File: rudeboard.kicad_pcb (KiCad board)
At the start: 2 copper layers, 295.8 x 124.2 mm, 132 parts, among them U1 Elite-C

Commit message: update to v1.1
changes to schematic:
- potentially better
- more pins used so more dependant on elite-c but more legible

routing:
- looks better than before
- is more dependant on elite-c (or much less on pro micro)

update revision/dates
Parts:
- moved U1 22.1 mm to (254.1, 140.5), turned to 270 degrees
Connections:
- D15 pad 1: row2 -> row0
- D16 pad 1: row3 -> row2
- D17 pad 1: row2 -> row3
- D18 pad 1: row3 -> row2
- D19 pad 1: row2 -> row3
- D20 pad 1: row3 -> row2
- D21 pad 1: row2 -> row3
- D22 pad 1: row3 -> row2
- D23 pad 1: row2 -> row3
- D24 pad 1: row3 -> row2
- D25 pad 1: row2 -> row3
- D26 pad 1: row3 -> row2
- D27 pad 1: row2 -> row3
- D28 pad 1: row3 -> row2
- D42 pad 1: row5 -> row7
- D54 pad 1: row7 -> row8
- D55 pad 1: row6 -> row9
- D56 pad 1: row7 -> row8
- D57 pad 1: row8 -> row9
- D58 pad 1: row9 -> row8
- D59 pad 1: row8 -> row9
- D60 pad 1: row9 -> row8
- D61 pad 1: row8 -> row9
- D62 pad 1: row9 -> row8
- D63 pad 1: row8 -> row10
- D64 pad 1: row9 -> row11
- D65 pad 1: row8 -> row10
- MX10 pad 1: col4 -> col5
- MX12 pad 1: col5 -> col6
- MX14 pad 1: col6 -> col7
- MX15 pad 1: col0 -> col7
- MX2 pad 1: col0 -> col1
- MX22 pad 1: col3 -> col4
- MX24 pad 1: col4 -> col5
- MX25 pad 1: col5 -> col6
- MX26 pad 1: col5 -> col6
- MX27 pad 1: col6 -> col7
- MX28 pad 1: col6 -> col7
- MX30 pad 1: col0 -> col1
- MX32 pad 1: col1 -> col2
- MX34 pad 1: col2 -> col3
- MX35 pad 1: col3 -> col4
- MX36 pad 1: col3 -> col4
- MX37 pad 1: col4 -> col5
- MX38 pad 1: col4 -> col6
- MX39 pad 1: col5 -> col6
- MX4 pad 1: col1 -> col2
- MX40 pad 1: col5 -> col7
- MX41 pad 1: col6 -> col7
- MX42 pad 1: col6 -> col0
- MX43 pad 1: col0 -> col1
- MX44 pad 1: col0 -> col1
- MX45 pad 1: col1 -> col2
- MX46 pad 1: col1 -> col2
- MX47 pad 1: col2 -> col3
- MX48 pad 1: col2 -> col4
- MX49 pad 1: col3 -> col5
- MX50 pad 1: col3 -> col6
- MX51 pad 1: col4 -> col6
- MX52 pad 1: col4 -> col7
- MX53 pad 1: col5 -> col7
- MX54 pad 1: col5 -> col1
- MX55 pad 1: col6 -> col1
- MX56 pad 1: col6 -> col2
- MX57 pad 1: col0 -> col2
- MX58 pad 1: col0 -> col3
- MX59 pad 1: col1 -> col5
- MX6 pad 1: col2 -> col3
- MX60 pad 1: col1 -> col6
- MX61 pad 1: col2 -> col6
- MX62 pad 1: col2 -> col7
- MX63 pad 1: col3 -> col2
- MX65 pad 1: col4 -> col6
- MX8 pad 1: col3 -> col4
- U1 pad 1: Net-(U1-Pad1) -> row0
- U1 pad 10: row3 -> col6
- U1 pad 11: row2 -> row8
- U1 pad 12: row0 -> row9
- U1 pad 13: col2 -> Net-(U1-Pad13)
- U1 pad 14: col6 -> Net-(U1-Pad14)
- U1 pad 15: Net-(U1-Pad15) -> row2
- U1 pad 16: col4 -> row3
- U1 pad 17: col3 -> col4
- U1 pad 18: row7 -> col3
- U1 pad 19: col1 -> col2
- U1 pad 2: Net-(U1-Pad2) -> row1
- U1 pad 20: col0 -> col1
- U1 pad 24: Net-(U1-Pad24) -> col0
- U1 pad 25: row1 -> row10
- U1 pad 26: Net-(U1-Pad26) -> row11
- U1 pad 27: Net-(U1-Pad27) -> col7
- U1 pad 29: col5 -> Net-(U1-Pad29)
- U1 pad 5: row8 -> row7
- U1 pad 6: row9 -> row6
- U1 pad 7: row6 -> row5
- U1 pad 8: row5 -> row4
- U1 pad 9: row4 -> col5
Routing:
- net col7: track 0.00 -> 281.2 mm, vias 0 -> 1
- net col5: track 397.1 -> 126.6 mm, vias 1 -> 0
- net col0: track 504.2 -> 279.5 mm, vias 0 -> 1
- net row10: track 0.00 -> 223.2 mm, vias 0 -> 1
- net col3: track 349.9 -> 189.8 mm, vias 2 -> 1
- net col6: track 396.0 -> 263.3 mm, vias 6 -> 1
- net row5: track 350.7 -> 264.3 mm, vias 8 -> 13
- net col4: track 246.6 -> 167.2 mm, vias 1 -> 0
- net row9: track 167.8 -> 238.7 mm, vias 5 -> 3
- net row7: track 340.0 -> 272.4 mm, vias 3 -> 0
- net col1: track 314.6 -> 375.0 mm, vias 0 -> 1
- net row11: track 0.00 -> 60.3 mm, vias 0 -> 1
- net row6: track 314.5 -> 263.3 mm, vias 4 -> 7
- net row3: track 339.7 -> 295.2 mm, vias 2 -> 13
- net row1: track 332.2 -> 292.9 mm, vias 3 -> 13
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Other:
- net class Default: clearance 0.2 -> 0.25
- rule trace_clearance: 0.2 -> 0.25
- rule trace_min: 0.2 -> 0.0889
- rule via_min_size: 0.4 -> 0.2

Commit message: prep for reroute
- delete all existing routes
- move all diodes to a side of the switch
- clean elite-c footprint
  - remove front silkscreen
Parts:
- moved U1 46.8 mm to (254.1, 93.7)
- moved D59 13.1 mm to (286.4, 150.6), turned to 90 degrees
- moved D47 13.1 mm to (210.2, 131.6), turned to 90 degrees
- moved D64 13.1 mm to (224.5, 169.8), turned to 90 degrees
- moved D63 13.0 mm to (129.2, 169.7), turned to 90 degrees
- moved D39 13.0 mm to (319.7, 112.5), turned to 90 degrees
- moved D51 13.0 mm to (319.7, 131.6), turned to 90 degrees
- moved D65 13.0 mm to (319.7, 169.7), turned to 90 degrees
- moved D44 13.0 mm to (129.2, 131.6), turned to 90 degrees
- moved D57 13.0 mm to (162.4, 150.6), turned to 90 degrees
- moved D61 12.9 mm to (329.1, 150.6), turned to 90 degrees
- moved D55 12.9 mm to (114.8, 150.6), turned to 90 degrees
- moved D16 12.9 mm to (90.9, 93.3), turned to 90 degrees
- moved D49 12.9 mm to (281.4, 131.4), turned to 90 degrees
- moved D12 12.9 mm to (300.5, 74.4), turned to 90 degrees
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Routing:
- net col1: track 375.0 -> 0.00 mm, vias 1 -> 0
- net row2: track 346.0 -> 0.00 mm, vias 1 -> 0
- net row0: track 341.5 -> 0.00 mm, vias 1 -> 0
- net col2: track 333.8 -> 0.00 mm
- net row4: track 314.2 -> 0.00 mm, vias 1 -> 0
- net row8: track 297.2 -> 0.00 mm, vias 2 -> 0
- net row3: track 295.2 -> 0.00 mm, vias 13 -> 0
- net row1: track 292.9 -> 0.00 mm, vias 13 -> 0
- net col7: track 281.2 -> 0.00 mm, vias 1 -> 0
- net col0: track 279.5 -> 0.00 mm, vias 1 -> 0
- net row7: track 272.4 -> 0.00 mm
- net row5: track 264.3 -> 0.00 mm, vias 13 -> 0
- net col6: track 263.3 -> 0.00 mm, vias 1 -> 0
- net row6: track 263.3 -> 0.00 mm, vias 7 -> 0
- net row9: track 238.7 -> 0.00 mm, vias 3 -> 0
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
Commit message: rerouted pcb
- better placement of elite-c
- looks better
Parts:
- moved D64 0.25 mm to (224.5, 169.5)
- moved D22 0.13 mm to (224.3, 93.5)
- moved D23 0.13 mm to (243.3, 93.5)
- moved D24 0.13 mm to (281.4, 93.5)
- moved D25 0.13 mm to (300.5, 93.5)
- moved D26 0.13 mm to (319.5, 93.5)
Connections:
- U1 pad 10: col6 -> row11
- U1 pad 11: row8 -> row10
- U1 pad 15: row2 -> col4
- U1 pad 16: row3 -> col3
- U1 pad 17: col4 -> col2
- U1 pad 18: col3 -> col1
- U1 pad 19: col2 -> row2
- U1 pad 20: col1 -> row3
- U1 pad 25: row10 -> row8
- U1 pad 26: row11 -> row6
- U1 pad 27: col7 -> row7
- U1 pad 28: Net-(U1-Pad28) -> row4
- U1 pad 29: Net-(U1-Pad29) -> row5
- U1 pad 5: row7 -> Net-(U1-Pad5)
- U1 pad 6: row6 -> Net-(U1-Pad6)
- U1 pad 7: row5 -> col7
- U1 pad 8: row4 -> col6
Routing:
- net row8: track 0.00 -> 323.1 mm, vias 0 -> 1
- net col1: track 0.00 -> 318.0 mm
- net col2: track 0.00 -> 300.0 mm
- net row7: track 0.00 -> 297.7 mm, vias 0 -> 5
- net row4: track 0.00 -> 295.3 mm, vias 0 -> 1
- net row6: track 0.00 -> 294.6 mm, vias 0 -> 7
- net row0: track 0.00 -> 288.4 mm
- net row2: track 0.00 -> 286.6 mm
- net row9: track 0.00 -> 267.1 mm, vias 0 -> 7
- net row10: track 0.00 -> 266.7 mm, vias 0 -> 1
- net row1: track 0.00 -> 246.8 mm, vias 0 -> 13
- net row5: track 0.00 -> 245.4 mm, vias 0 -> 10
- net row3: track 0.00 -> 243.1 mm, vias 0 -> 10
- net col0: track 0.00 -> 241.3 mm, vias 0 -> 1
- net col6: track 0.00 -> 237.7 mm
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
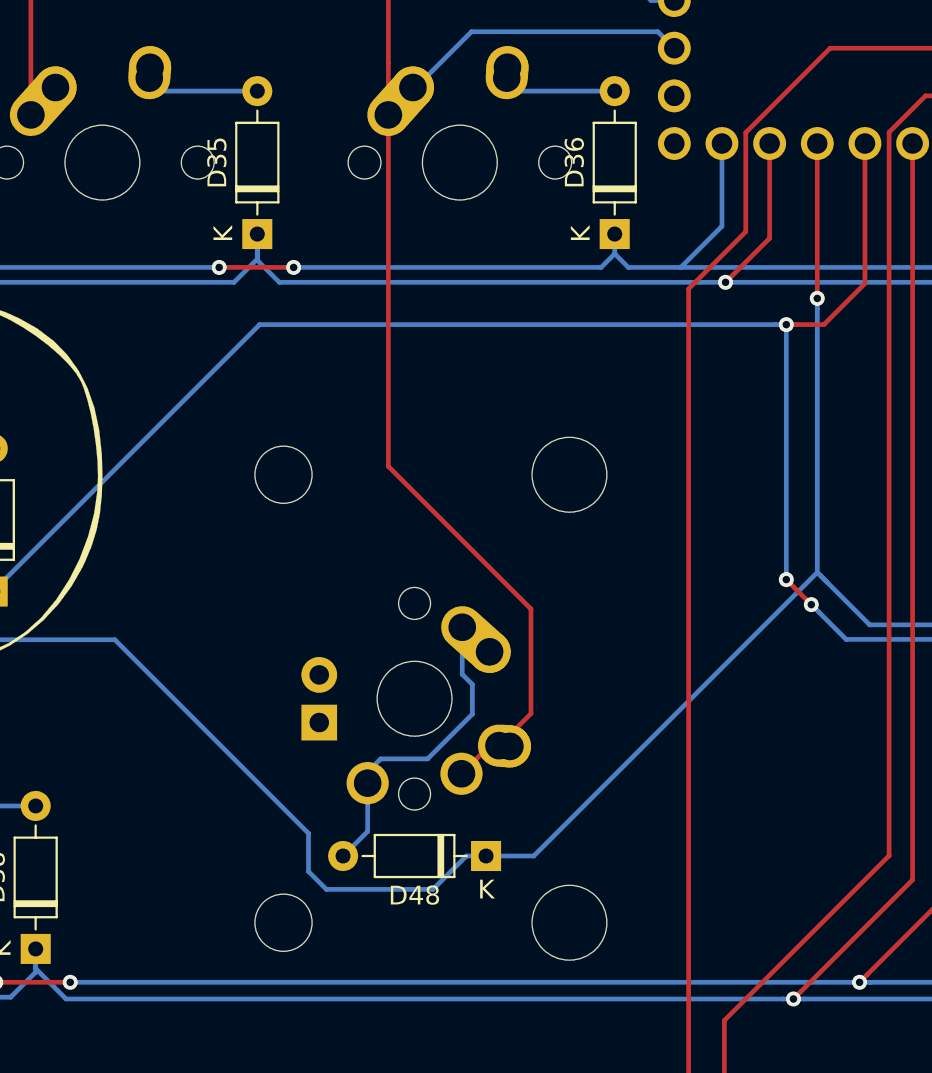
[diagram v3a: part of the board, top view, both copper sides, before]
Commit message: update iso enter to 0deg rotated
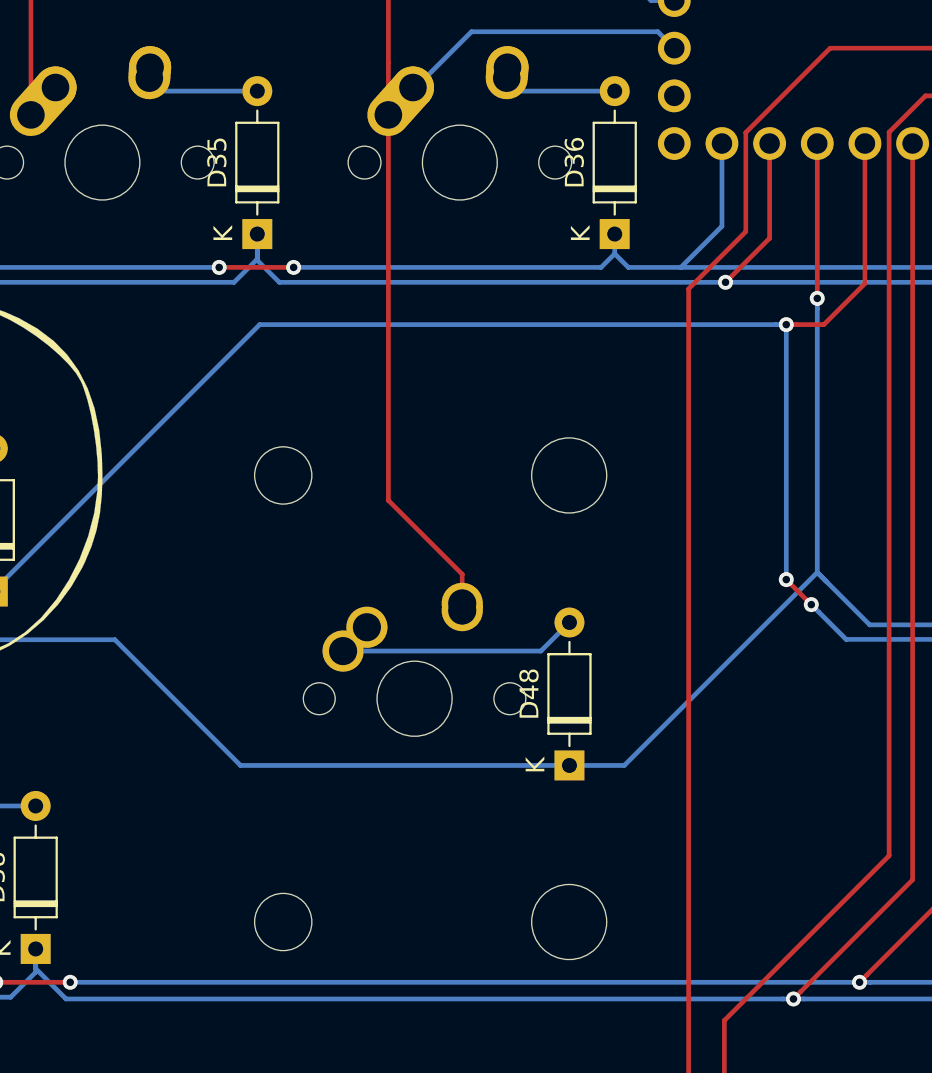
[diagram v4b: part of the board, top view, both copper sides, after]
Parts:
- MX48: footprint MX_Alps_Hybrid:MX-ISO -> Button_Switch_Keyboard:SW_Cherry_MX_ISOEnter_PCB
- moved D48 6.56 mm to (240.9, 140.8), turned to 90 degrees
- moved MX48 5.68 mm to (235.2, 132.2)
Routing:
- net col4: track 153.3 -> 140.4 mm
- net row7: track 297.7 -> 291.1 mm
- net Net-(D48-Pad2): track 16.7 -> 14.5 mm

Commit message: v1.2
- using traditional matrix -- duplex matrix didn't provide any benifit
- still dependant on elite-c
- much better looking pcb
- everything else is same
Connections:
- D1 pad 1: row0 -> /row0
- D10 pad 1: row1 -> /row0
- D11 pad 1: row0 -> /row0
- D12 pad 1: row1 -> /row0
- D13 pad 1: row0 -> /row0
- D14 pad 1: row1 -> /row0
- D15 pad 1: row0 -> /row0
- D16 pad 1: row2 -> /row1
- D17 pad 1: row3 -> /row1
- D18 pad 1: row2 -> /row1
- D19 pad 1: row3 -> /row1
- D2 pad 1: row1 -> /row0
- D20 pad 1: row2 -> /row1
- D21 pad 1: row3 -> /row1
- D22 pad 1: row2 -> /row1
- D23 pad 1: row3 -> /row1
- D24 pad 1: row2 -> /row1
- D25 pad 1: row3 -> /row1
- D26 pad 1: row2 -> /row1
- D27 pad 1: row3 -> /row1
- D28 pad 1: row2 -> /row1
- D29 pad 1: row4 -> /row2
- D3 pad 1: row0 -> /row0
- D30 pad 1: row5 -> /row2
- D31 pad 1: row4 -> /row2
- D32 pad 1: row5 -> /row2
- D33 pad 1: row4 -> /row2
- D34 pad 1: row5 -> /row2
- D35 pad 1: row4 -> /row2
- D36 pad 1: row5 -> /row2
- D37 pad 1: row4 -> /row2
- D38 pad 1: row5 -> /row2
- D39 pad 1: row4 -> /row2
- D4 pad 1: row1 -> /row0
- D40 pad 1: row5 -> /row2
- D41 pad 1: row4 -> /row2
- D42 pad 1: row7 -> /row3
- D43 pad 1: row6 -> /row3
- D44 pad 1: row7 -> /row3
- D45 pad 1: row6 -> /row3
- D46 pad 1: row7 -> /row3
- D47 pad 1: row6 -> /row3
- D48 pad 1: row7 -> /row3
- D49 pad 1: row6 -> /row3
- D5 pad 1: row0 -> /row0
- D50 pad 1: row7 -> /row3
- D51 pad 1: row6 -> /row3
- D52 pad 1: row7 -> /row3
- D53 pad 1: row6 -> /row3
- D54 pad 1: row8 -> /row4
- D55 pad 1: row9 -> /row4
- D56 pad 1: row8 -> /row4
- D57 pad 1: row9 -> /row4
- D58 pad 1: row8 -> /row4
- D59 pad 1: row9 -> /row4
- D6 pad 1: row1 -> /row0
- D60 pad 1: row8 -> /row4
- D61 pad 1: row9 -> /row4
- D62 pad 1: row8 -> /row4
- D63 pad 1: row10 -> /row5
- D64 pad 1: row11 -> /row5
- D65 pad 1: row10 -> /row5
- D7 pad 1: row0 -> /row0
- D8 pad 1: row1 -> /row0
- D9 pad 1: row0 -> /row0
- MX1 pad 1: col0 -> /col0
- MX10 pad 1: col5 -> /col9
- MX11 pad 1: col5 -> /col10
- MX12 pad 1: col6 -> /col11
- MX13 pad 1: col6 -> /col12
- MX14 pad 1: col7 -> /col13
- MX15 pad 1: col7 -> /col14
- MX16 pad 1: col0 -> /col0
- MX17 pad 1: col1 -> /col1
- MX18 pad 1: col1 -> /col2
- MX19 pad 1: col2 -> /col3
- MX2 pad 1: col1 -> /col1
- MX20 pad 1: col2 -> /col4
- MX21 pad 1: col3 -> /col6
- MX22 pad 1: col4 -> /col7
- MX23 pad 1: col4 -> /col8
- MX24 pad 1: col5 -> /col10
- MX25 pad 1: col6 -> /col11
- MX26 pad 1: col6 -> /col12
- MX27 pad 1: col7 -> /col13
- MX28 pad 1: col7 -> /col14
- MX29 pad 1: col0 -> /col0
- MX3 pad 1: col1 -> /col2
- MX30 pad 1: col1 -> /col1
- MX31 pad 1: col1 -> /col2
- MX32 pad 1: col2 -> /col3
- MX33 pad 1: col2 -> /col4
- MX34 pad 1: col3 -> /col6
- MX35 pad 1: col4 -> /col7
- MX36 pad 1: col4 -> /col8
- MX37 pad 1: col5 -> /col10
- MX38 pad 1: col6 -> /col11
- MX39 pad 1: col6 -> /col12
- MX4 pad 1: col2 -> /col3
- MX40 pad 1: col7 -> /col13
- MX41 pad 1: col7 -> /col14
- MX42 pad 1: col0 -> /col0
- MX43 pad 1: col1 -> /col1
- MX44 pad 1: col1 -> /col2
- MX45 pad 1: col2 -> /col3
- MX46 pad 1: col2 -> /col4
- MX47 pad 1: col3 -> /col6
- MX48 pad 1: col4 -> /col8
- MX49 pad 1: col5 -> /col10
- MX5 pad 1: col2 -> /col4
- MX50 pad 1: col6 -> /col11
- MX51 pad 1: col6 -> /col12
- MX52 pad 1: col7 -> /col13
- MX53 pad 1: col7 -> /col14
- MX54 pad 1: col1 -> /col1
- MX55 pad 1: col1 -> /col2
- MX56 pad 1: col2 -> /col3
- MX57 pad 1: col2 -> /col4
- MX58 pad 1: col3 -> /col6
- MX59 pad 1: col5 -> /col10
- MX6 pad 1: col3 -> /col5
- MX60 pad 1: col6 -> /col11
- MX61 pad 1: col6 -> /col12
- MX62 pad 1: col7 -> /col13
- MX63 pad 1: col2 -> /col3
- MX64 pad 1: col3 -> /col6
- MX65 pad 1: col6 -> /col11
- MX7 pad 1: col3 -> /col6
- MX8 pad 1: col4 -> /col7
- MX9 pad 1: col4 -> /col8
- U1 pad 1: row0 -> /col5
- U1 pad 10: row11 -> /col12
- U1 pad 11: row10 -> /col8
- U1 pad 12: row9 -> /col11
- U1 pad 13: Net-(U1-Pad13) -> /col7
- U1 pad 14: Net-(U1-Pad14) -> /col6
- U1 pad 15: col4 -> /col4
- U1 pad 16: col3 -> /col3
- U1 pad 17: col2 -> /col2
- U1 pad 18: col1 -> /col1
- U1 pad 19: row2 -> /col0
- U1 pad 2: row1 -> /col9
- U1 pad 20: row3 -> /row1
- U1 pad 24: col0 -> /row0
- U1 pad 25: row8 -> /col10
- U1 pad 26: row6 -> /row4
- U1 pad 27: row7 -> /row5
- U1 pad 28: row4 -> /row3
- U1 pad 29: row5 -> /row2
- U1 pad 7: col7 -> Net-(U1-Pad7)
- U1 pad 8: col6 -> /col14
- U1 pad 9: col5 -> /col13
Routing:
- net row8: track 323.1 -> 0.00 mm, vias 1 -> 0
- net col1: track 318.0 -> 0.00 mm
- net /row4: track 0.00 -> 310.1 mm, vias 0 -> 1
- net col2: track 300.0 -> 0.00 mm
- net /row3: track 0.00 -> 299.4 mm, vias 0 -> 1
- net row4: track 295.3 -> 0.00 mm, vias 1 -> 0
- net row6: track 294.6 -> 0.00 mm, vias 7 -> 0
- net row7: track 291.1 -> 0.00 mm, vias 5 -> 0
- net row0: track 288.4 -> 0.00 mm
- net row2: track 286.6 -> 0.00 mm
- net /row2: track 0.00 -> 273.5 mm
- net /row0: track 0.00 -> 273.3 mm
- net /row1: track 0.00 -> 270.3 mm
- net row9: track 267.1 -> 0.00 mm, vias 7 -> 0
- net row10: track 266.7 -> 0.00 mm, vias 1 -> 0
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
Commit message: route pcb for integrated mcu
- includes spi pin breakout
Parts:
- removed G***: LOGO, Keebio_Parts:SquirtleSquadLeader
- added C1: 22pF, Capacitor_SMD:C_0805_2012Metric_Pad1.15x1.40mm_HandSolder, B.Cu at (261.7, 102.1)
- added C2: 22pF, Capacitor_SMD:C_0805_2012Metric_Pad1.15x1.40mm_HandSolder, B.Cu at (267.5, 96.4)
- added C3: 1uF, Capacitor_SMD:C_0805_2012Metric_Pad1.15x1.40mm_HandSolder, B.Cu at (262.2, 85.4)
- added C4: 0.1uF, Capacitor_SMD:C_0805_2012Metric_Pad1.15x1.40mm_HandSolder, B.Cu at (252.7, 114.8)
- added C5: 0.1uF, Capacitor_SMD:C_0805_2012Metric_Pad1.15x1.40mm_HandSolder, B.Cu at (256.0, 114.8)
- added C6: 0.1uF, Capacitor_SMD:C_0805_2012Metric_Pad1.15x1.40mm_HandSolder, B.Cu at (254.4, 111.0)
- added C7: 10F, Capacitor_SMD:C_0805_2012Metric_Pad1.15x1.40mm_HandSolder, B.Cu at (254.4, 107.6)
- added F1: 500mA, Fuse:Fuse_1206_3216Metric_Pad1.42x1.75mm_HandSolder, B.Cu at (86.4, 61.0)
- added J1: Conn_01x04, Connector_PinHeader_2.54mm:PinHeader_1x04_P2.54mm_Vertical, B.Cu at (261.0, 58.5)
- added J2: USB_B_Mini, Keebio-Parts:USB-Mini-B_ LCSC-C46398, B.Cu at (93.3, 63.2)
- added R1: 10k, Resistor_SMD:R_0805_2012Metric_Pad1.15x1.40mm_HandSolder, B.Cu at (269.2, 94.8)
- added R2: 22, Resistor_SMD:R_0805_2012Metric_Pad1.15x1.40mm_HandSolder, B.Cu at (100.1, 63.1)
- added R3: 22, Resistor_SMD:R_0805_2012Metric_Pad1.15x1.40mm_HandSolder, B.Cu at (94.2, 66.9)
- added R4: 10k, Resistor_SMD:R_0805_2012Metric_Pad1.15x1.40mm_HandSolder, B.Cu at (246.9, 102.5)
- added SW1: SW_Push, Button_Switch_SMD:SW_SPST_SKQG_WithStem, B.Cu at (307.8, 97.0)
- added Y1: 16MHz, Crystal:Crystal_SMD_3225-4Pin_3.2x2.5mm, B.Cu at (264.2, 99.3)
- U1: value Elite-C -> ATmega32U4-AU; footprint Keebio_Parts:Elite-C -> Package_QFP:TQFP-44_10x10mm_P0.8mm
- moved U1 1.94 mm to (256.0, 93.3), turned to 225 degrees
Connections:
- U1 pad 10: /col12 -> /MOSI
- U1 pad 11: /col8 -> /MISO
- U1 pad 12: /col11 -> /col14
- U1 pad 13: /col7 -> Net-(R1-Pad2)
- U1 pad 14: /col6 -> +5V
- U1 pad 15: /col4 -> GND
- U1 pad 16: /col3 -> Net-(C2-Pad1)
- U1 pad 17: /col2 -> Net-(C1-Pad1)
- U1 pad 18: /col1 -> /col13
- U1 pad 19: /col0 -> /col12
- U1 pad 2: /col9 -> +5V
- U1 pad 20: /row1 -> /col8
- U1 pad 21: Net-(U1-Pad21) -> /col9
- U1 pad 22: Net-(U1-Pad22) -> /col11
- U1 pad 23: Net-(U1-Pad23) -> GND
- U1 pad 24: /row0 -> +5V
- U1 pad 5: Net-(U1-Pad5) -> GND
- U1 pad 7: Net-(U1-Pad7) -> +5V
- U1 pad 8: /col14 -> /SS
- U1 pad 9: /col13 -> /SCK
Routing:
- net Net-(R3-Pad2): track 0.00 -> 185.2 mm, vias 0 -> 4
- net Net-(R2-Pad1): track 0.00 -> 180.9 mm, vias 0 -> 2
- net GND: track 0.00 -> 52.1 mm, vias 0 -> 8
- net Net-(R1-Pad2): track 0.00 -> 51.5 mm
- net +5V: track 0.00 -> 51.0 mm, vias 0 -> 10
- net /MISO: track 0.00 -> 36.0 mm, vias 0 -> 1
- net /MOSI: track 0.00 -> 34.6 mm, vias 0 -> 1
- net /SS: track 0.00 -> 34.1 mm, vias 0 -> 1
- net /SCK: track 0.00 -> 33.8 mm, vias 0 -> 1
- net /row2: track 273.5 -> 290.4 mm, vias 0 -> 1
- net /row3: track 299.4 -> 314.5 mm, vias 1 -> 2
- net /row0: track 273.3 -> 287.1 mm
- net /col9: track 21.3 -> 35.0 mm, vias 2 -> 1
- net /row5: track 254.2 -> 266.7 mm, vias 1 -> 2
- net /col10: track 105.0 -> 117.2 mm, vias 0 -> 1
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- added copper zone on F.Cu, net +5V
- added copper zone on B.Cu, net GND
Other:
- net class power added: clearance 0.25, trace_width 0.381, via_dia 0.8, via_drill 0.4
- board text added: "MI"
- board text added: "MO"
- board text added: "SC"
- board text added: "SS"
- board text removed: "rudeboard"
